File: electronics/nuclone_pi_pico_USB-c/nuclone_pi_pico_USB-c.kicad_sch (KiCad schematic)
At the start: 19 parts, among them J1 JTAG_2X05, J3 nuclone_medium_left, J4 nuclone_medium_right

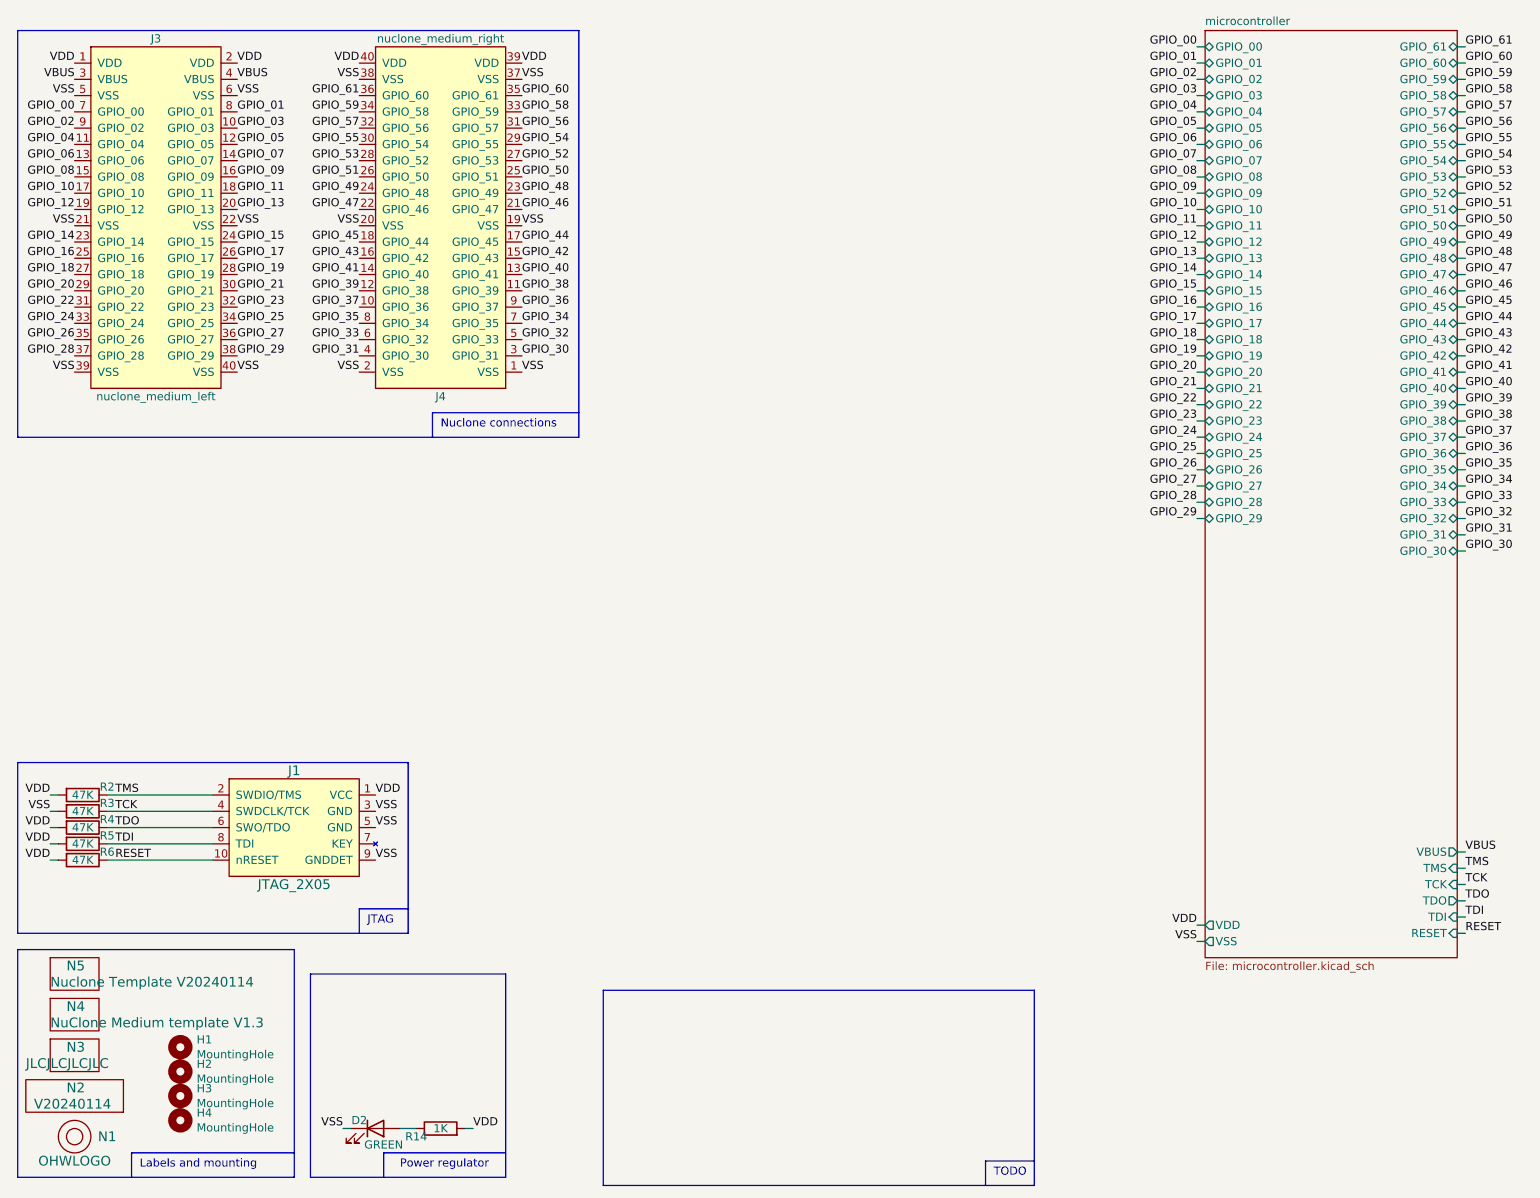
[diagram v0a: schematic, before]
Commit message: added USB-C connection, routing and placing bits and pieces
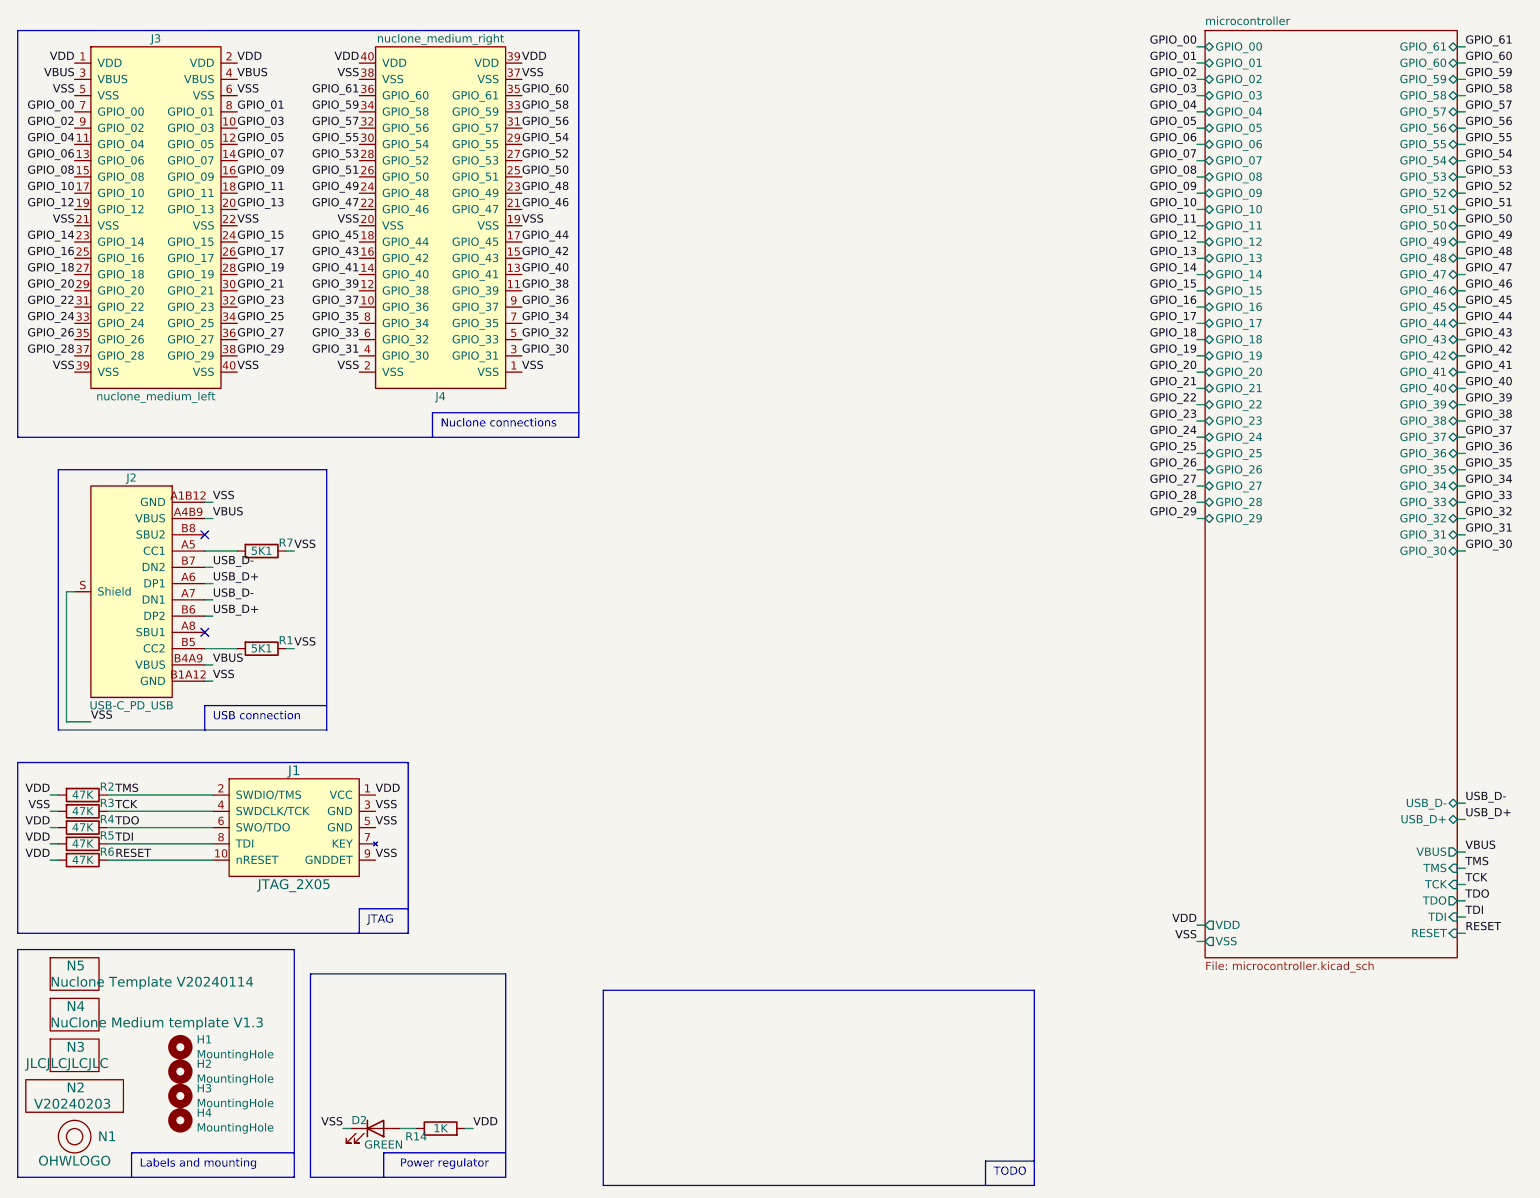
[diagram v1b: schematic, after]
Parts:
- added J2: USB-C_PD_USB, SquantorUsb:USB-C-HRO-31-M-12_aisler, symbol SquantorUsb:USB-C_PD_USB
- added R1, R7: 5K1, SquantorResistor:R_0603_hand, symbol Device:R
- N2: value V20240114 -> V20240203
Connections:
- net VBUS: now also J2.A4B9 (VBUS), J2.B4A9 (VBUS)
- net VSS: now also J2.A1B12 (GND), J2.B1A12 (GND), J2.S (Shield), R1.1, R7.1
- new net: J2.A5 (CC1), R7.2
- new net: J2.B5 (CC2), R1.2
- new net USB_D+: J2.A6 (DP1), J2.B6 (DP2)
- new net USB_D-: J2.A7 (DN1), J2.B7 (DN2)
- no-connect marks 0 -> 2
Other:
- sheet microcontroller ports: added USB_D+, USB_D-; removed none
- note added: "USB connection"

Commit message: moved pico down more, changed routing
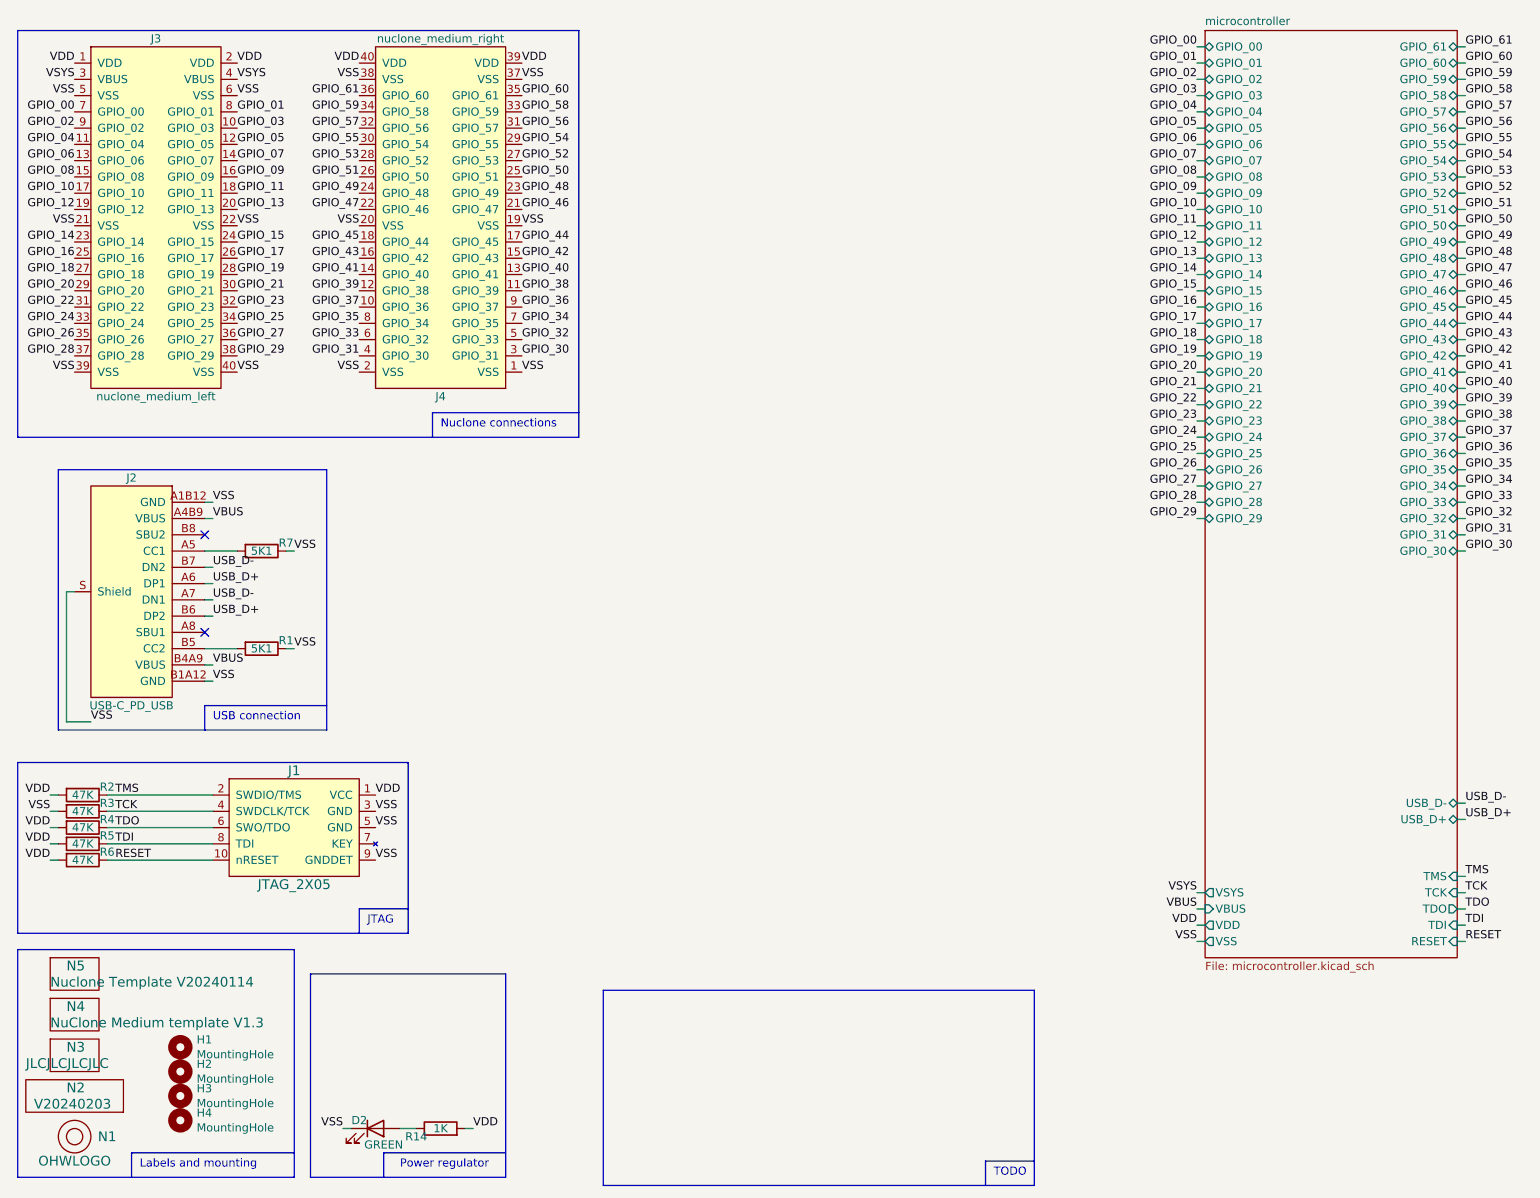
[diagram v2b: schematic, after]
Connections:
- net VBUS: no longer J3.3 (VBUS), J3.4 (VBUS)
- new net VSYS: J3.3 (VBUS), J3.4 (VBUS)
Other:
- sheet microcontroller ports: added VSYS; removed none
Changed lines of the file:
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@@
-    (stroke (width 0) (type default))
-  )
-  (wire (pts (xy 240.03 143.51) (xy 241.3 143.51))
     (stroke (width 0) (type default))
   )
@@
     (stroke (width 0) (type default))
   )
+  (wire (pts (xy 199.39 152.4) (xy 200.66 152.4))
+    (stroke (width 0) (type default))
+  )
   (wire (pts (xy 199.39 154.94) (xy 200.66 154.94))
     (stroke (width 0) (type default))
@@
     (stroke (width 0) (type default))
   )
+  (wire (pts (xy 199.39 149.86) (xy 200.66 149.86))
+    (stroke (width 0) (type default))
+  )
   (wire (pts (xy 240.03 83.82) (xy 241.3 83.82))
     (stroke (width 0) (type default))
@@
     (stroke (width 0) (type default))
   )
-  (wire (pts (xy 240.03 151.13) (xy 241.3 151.13))
+  (wire (pts (xy 240.03 152.4) (xy 241.3 152.4))
     (stroke (width 0) (type default))
   )
@@
     (stroke (width 0) (type default))
   )
-  (wire (pts (xy 240.03 153.67) (xy 241.3 153.67))
+  (wire (pts (xy 240.03 154.94) (xy 241.3 154.94))
     (stroke (width 0) (type default))
   )
@@
     (stroke (width 0) (type default))
   )
-  (wire (pts (xy 240.03 156.21) (xy 241.3 156.21))
+  (wire (pts (xy 240.03 157.48) (xy 241.3 157.48))
     (stroke (width 0) (type default))
   )
@@
     (stroke (width 0) (type default))
   )
-  (wire (pts (xy 240.03 146.05) (xy 241.3 146.05))
+  (wire (pts (xy 240.03 147.32) (xy 241.3 147.32))
     (stroke (width 0) (type default))
   )
@@
     (stroke (width 0) (type default))
   )
-  (wire (pts (xy 240.03 148.59) (xy 241.3 148.59))
+  (wire (pts (xy 240.03 149.86) (xy 241.3 149.86))
     (stroke (width 0) (type default))
   )
@@
     (effects (font (size 1.27 1.27)) (justify right bottom))
   )
-  (label "VBUS" (at 241.3 143.51 0) (fields_autoplaced)
-    (effects (font (size 1.27 1.27)) (justify left bottom))
+  (label "VBUS" (at 199.39 152.4 180) (fields_autoplaced)
+    (effects (font (size 1.27 1.27)) (justify right bottom))
   )
   (label "VSS" (at 199.39 157.48 180) (fields_autoplaced)
@@
     (effects (font (size 1.27 1.27)) (justify left bottom))
   )
-  (label "VBUS" (at 49.53 22.86 0) (fields_autoplaced)
-    (effects (font (size 1.27 1.27)) (justify left bottom))
-  )
   (label "GPIO_44" (at 241.3 60.96 0) (fields_autoplaced)
     (effects (font (size 1.27 1.27)) (justify left bottom))
@@
     (effects (font (size 1.27 1.27)) (justify right bottom))
   )
-  (label "TDI" (at 241.3 153.67 0) (fields_autoplaced)
+  (label "TDI" (at 241.3 154.94 0) (fields_autoplaced)
     (effects (font (size 1.27 1.27)) (justify left bottom))
   )
@@
     (effects (font (size 1.27 1.27)) (justify left bottom))
   )
+  (label "VSYS" (at 49.53 22.86 0) (fields_autoplaced)
+    (effects (font (size 1.27 1.27)) (justify left bottom))
+  )
   (label "GPIO_13" (at 199.39 50.8 180) (fields_autoplaced)
     (effects (font (size 1.27 1.27)) (justify right bottom))
@@
     (effects (font (size 1.27 1.27)) (justify left bottom))
   )
-  (label "TCK" (at 241.3 148.59 0) (fields_autoplaced)
+  (label "TCK" (at 241.3 149.86 0) (fields_autoplaced)
     (effects (font (size 1.27 1.27)) (justify left bottom))
   )
@@
     (effects (font (size 1.27 1.27)) (justify left bottom))
   )
-  (label "TMS" (at 241.3 146.05 0) (fields_autoplaced)
+  (label "TMS" (at 241.3 147.32 0) (fields_autoplaced)
     (effects (font (size 1.27 1.27)) (justify left bottom))
   )
@@
     (effects (font (size 1.27 1.27)) (justify right bottom))
   )
-  (label "TDO" (at 241.3 151.13 0) (fields_autoplaced)
+  (label "TDO" (at 241.3 152.4 0) (fields_autoplaced)
     (effects (font (size 1.27 1.27)) (justify left bottom))
   )
@@
     (effects (font (size 1.27 1.27)) (justify right bottom))
   )
+  (label "VSYS" (at 24.13 22.86 180) (fields_autoplaced)
+    (effects (font (size 1.27 1.27)) (justify right bottom))
+  )
   (label "GPIO_09" (at 49.53 38.1 0) (fields_autoplaced)
     (effects (font (size 1.27 1.27)) (justify left bottom))
@@
     (effects (font (size 1.27 1.27)) (justify left bottom))
   )
+  (label "VSYS" (at 199.39 149.86 180) (fields_autoplaced)
+    (effects (font (size 1.27 1.27)) (justify right bottom))
+  )
   (label "GPIO_03" (at 199.39 25.4 180) (fields_autoplaced)
     (effects (font (size 1.27 1.27)) (justify right bottom))
@@
     (effects (font (size 1.27 1.27)) (justify left bottom))
   )
-  (label "VBUS" (at 24.13 22.86 180) (fields_autoplaced)
-    (effects (font (size 1.27 1.27)) (justify right bottom))
-  )
   (label "RESET" (at 30.48 144.78 0) (fields_autoplaced)
     (effects (font (size 1.27 1.27)) (justify left bottom))
@@
     (effects (font (size 1.27 1.27)) (justify right bottom))
   )
-  (label "RESET" (at 241.3 156.21 0) (fields_autoplaced)
+  (label "RESET" (at 241.3 157.48 0) (fields_autoplaced)
     (effects (font (size 1.27 1.27)) (justify left bottom))
   )
@@
       (effects (font (size 1.27 1.27)) (justify left top))
     )
-    (pin "TMS" input (at 240.03 146.05 0)
-      (effects (font (size 1.27 1.27)) (justify right))
-    )
-    (pin "TCK" input (at 240.03 148.59 0)
-      (effects (font (size 1.27 1.27)) (justify right))
-    )
-    (pin "TDI" input (at 240.03 153.67 0)
-      (effects (font (size 1.27 1.27)) (justify right))
-    )
-    (pin "TDO" output (at 240.03 151.13 0)
-      (effects (font (size 1.27 1.27)) (justify right))
-    )
-    (pin "RESET" input (at 240.03 156.21 0)
+    (pin "TMS" input (at 240.03 147.32 0)
+      (effects (font (size 1.27 1.27)) (justify right))
+    )
+    (pin "TCK" input (at 240.03 149.86 0)
+      (effects (font (size 1.27 1.27)) (justify right))
+    )
+    (pin "TDI" input (at 240.03 154.94 0)
+      (effects (font (size 1.27 1.27)) (justify right))
+    )
+    (pin "TDO" output (at 240.03 152.4 0)
+      (effects (font (size 1.27 1.27)) (justify right))
+    )
+    (pin "RESET" input (at 240.03 157.48 0)
       (effects (font (size 1.27 1.27)) (justify right))
     )
@@
       (effects (font (size 1.27 1.27)) (justify right))
     )
-    (pin "VBUS" output (at 240.03 143.51 0)
-      (effects (font (size 1.27 1.27)) (justify right))
-    )
     (pin "VSS" output (at 200.66 157.48 180)
       (effects (font (size 1.27 1.27)) (justify left))
@@
       (effects (font (size 1.27 1.27)) (justify right))
     )
-    (instances
+    (pin "VSYS" output (at 200.66 149.86 180)
+      (effects (font (size 1.27 1.27)) (justify left))
+    )
+    (pin "VBUS" input (at 200.66 152.4 180)
+      (effects (font (size 1.27 1.27)) (justify left))
+    )
+    (instances

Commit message: minor additions
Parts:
- N4: value NuClone Medium template V1.3 -> Raspberry Pi Pico USB-C
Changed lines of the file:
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@@
       (effects (font (size 1.524 1.524)) (justify left))
     )
-    (property "Value" "NuClone Medium template V1.3" (at 20.32 170.18 0)
+    (property "Value" "Raspberry Pi Pico USB-C" (at 20.32 170.18 0)
       (effects (font (size 1.524 1.524)) (justify left))
     )

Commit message: small trace updates
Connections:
- net GPIO_30: now also J4.4 (GPIO_30); no longer J4.3 (GPIO_31)
- net GPIO_31: now also J4.3 (GPIO_31); no longer J4.4 (GPIO_30)
- net GPIO_32: now also J4.6 (GPIO_32); no longer J4.5 (GPIO_33)
- net GPIO_33: now also J4.5 (GPIO_33); no longer J4.6 (GPIO_32)
- net GPIO_34: now also J4.8 (GPIO_34); no longer J4.7 (GPIO_35)
- net GPIO_35: now also J4.7 (GPIO_35); no longer J4.8 (GPIO_34)
- net GPIO_36: now also J4.10 (GPIO_36); no longer J4.9 (GPIO_37)
- net GPIO_37: now also J4.9 (GPIO_37); no longer J4.10 (GPIO_36)
- net GPIO_38: now also J4.12 (GPIO_38); no longer J4.11 (GPIO_39)
- net GPIO_39: now also J4.11 (GPIO_39); no longer J4.12 (GPIO_38)
- net GPIO_40: now also J4.14 (GPIO_40); no longer J4.13 (GPIO_41)
- net GPIO_41: now also J4.13 (GPIO_41); no longer J4.14 (GPIO_40)
- net GPIO_42: now also J4.16 (GPIO_42); no longer J4.15 (GPIO_43)
- net GPIO_43: now also J4.15 (GPIO_43); no longer J4.16 (GPIO_42)
- net GPIO_44: now also J4.18 (GPIO_44); no longer J4.17 (GPIO_45)
- net GPIO_45: now also J4.17 (GPIO_45); no longer J4.18 (GPIO_44)
- net GPIO_46: now also J4.22 (GPIO_46); no longer J4.21 (GPIO_47)
- net GPIO_47: now also J4.21 (GPIO_47); no longer J4.22 (GPIO_46)
- net GPIO_48: now also J4.24 (GPIO_48); no longer J4.23 (GPIO_49)
- net GPIO_49: now also J4.23 (GPIO_49); no longer J4.24 (GPIO_48)
- net GPIO_50: now also J4.26 (GPIO_50); no longer J4.25 (GPIO_51)
- net GPIO_51: now also J4.25 (GPIO_51); no longer J4.26 (GPIO_50)
- net GPIO_52: now also J4.28 (GPIO_52); no longer J4.27 (GPIO_53)
- net GPIO_53: now also J4.27 (GPIO_53); no longer J4.28 (GPIO_52)
- net GPIO_54: now also J4.30 (GPIO_54); no longer J4.29 (GPIO_55)
- net GPIO_55: now also J4.29 (GPIO_55); no longer J4.30 (GPIO_54)
- net GPIO_56: now also J4.32 (GPIO_56); no longer J4.31 (GPIO_57)
- net GPIO_57: now also J4.31 (GPIO_57); no longer J4.32 (GPIO_56)
- net GPIO_58: now also J4.34 (GPIO_58); no longer J4.33 (GPIO_59)
- net GPIO_59: now also J4.33 (GPIO_59); no longer J4.34 (GPIO_58)
- net GPIO_60: now also J4.36 (GPIO_60); no longer J4.35 (GPIO_61)
- net GPIO_61: now also J4.35 (GPIO_61); no longer J4.36 (GPIO_60)

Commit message: prepping for production, updated footprint and versionnumber
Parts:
- N2: value V20240203 -> V20240218
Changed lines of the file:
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@@
       (effects (font (size 1.524 1.524)) (justify left))
     )
-    (property "Value" "V20240203" (at 17.78 182.88 0)
+    (property "Value" "V20240218" (at 17.78 182.88 0)
       (effects (font (size 1.524 1.524)) (justify left))
     )

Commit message: reviewed and updated PCB library
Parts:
- N2: value V20240218 -> V20240424
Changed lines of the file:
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@@
       (effects (font (size 1.524 1.524)) (justify left))
     )
-    (property "Value" "V20240218" (at 17.78 182.88 0)
+    (property "Value" "V20240424" (at 17.78 182.88 0)
       (effects (font (size 1.524 1.524)) (justify left))
     )

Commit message: preparing for production final checks
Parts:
- N2: value V20240424 -> V20240426
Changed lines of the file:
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@@
       (effects (font (size 1.524 1.524)) (justify left))
     )
-    (property "Value" "V20240424" (at 17.78 182.88 0)
+    (property "Value" "V20240426" (at 17.78 182.88 0)
       (effects (font (size 1.524 1.524)) (justify left))
     )
